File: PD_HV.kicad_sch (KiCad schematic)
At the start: 0 parts

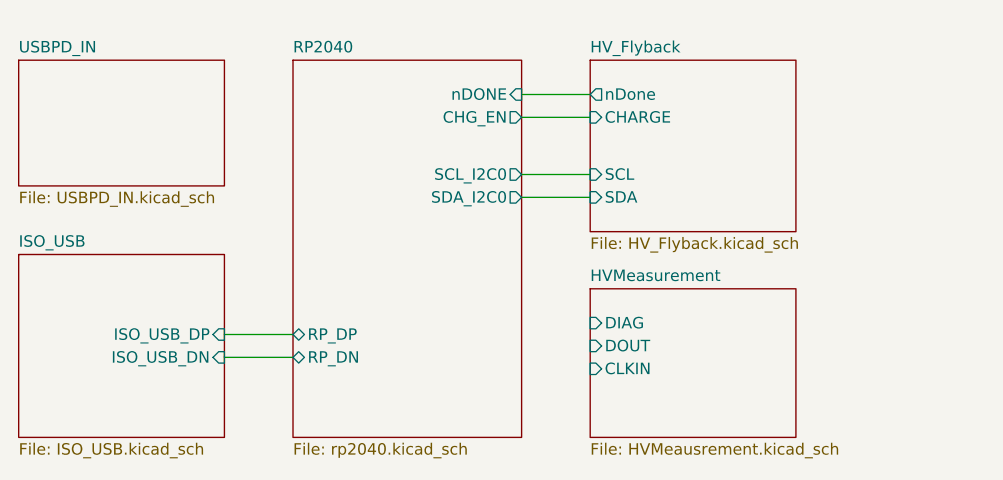
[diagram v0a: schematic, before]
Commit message: finished routing, sending to fab
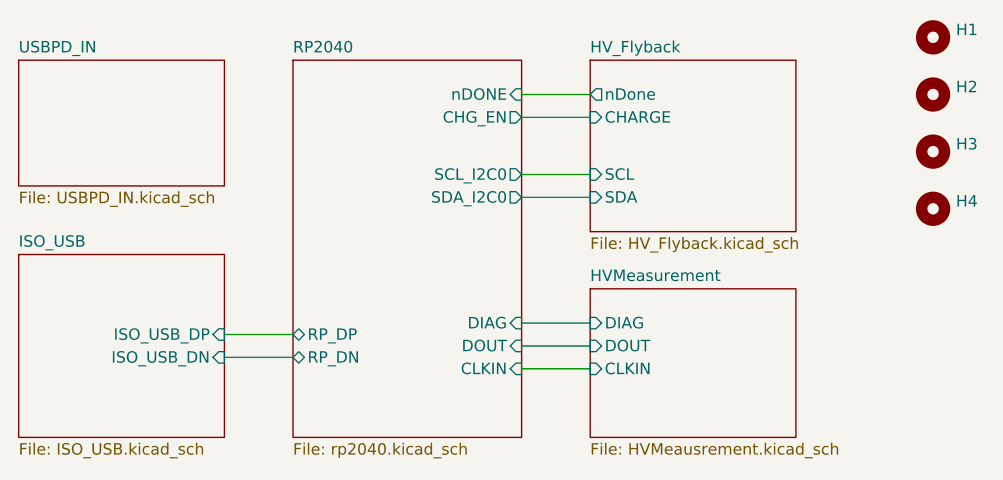
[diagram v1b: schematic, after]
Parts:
- added H1, H2, H3, H4: (no value), symbol Mechanical:MountingHole
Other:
- sheet RP2040 ports: added CLKIN, DIAG, DOUT; removed none
